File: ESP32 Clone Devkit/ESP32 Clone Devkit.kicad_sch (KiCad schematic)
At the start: 34 parts, among them J1 USB_B_Micro, J2 Conn_01x19_Pin, J3 Conn_01x19_Pin, Q1 MMSS8050-H-TP, Q2 MMSS8050-H-TP, SW1 SW_Push, SW2 SW_Push, U1 CP2102N-A02-GQFN28, U2 AMS1117-3.3

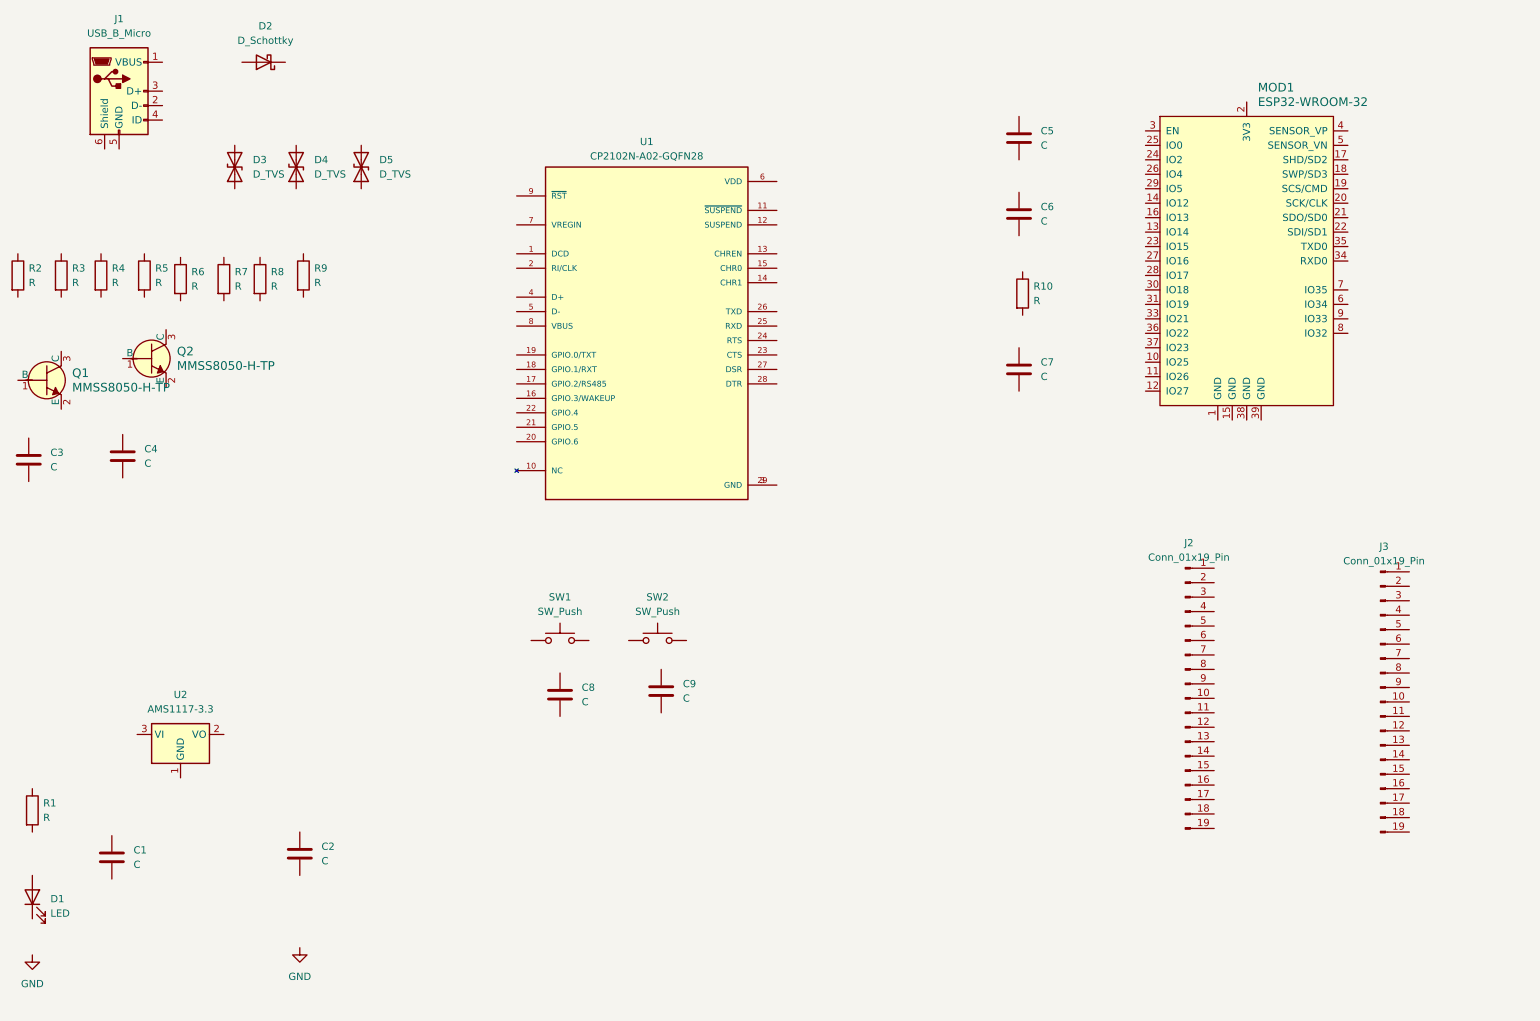
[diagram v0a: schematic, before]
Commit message: Annotate and set components values
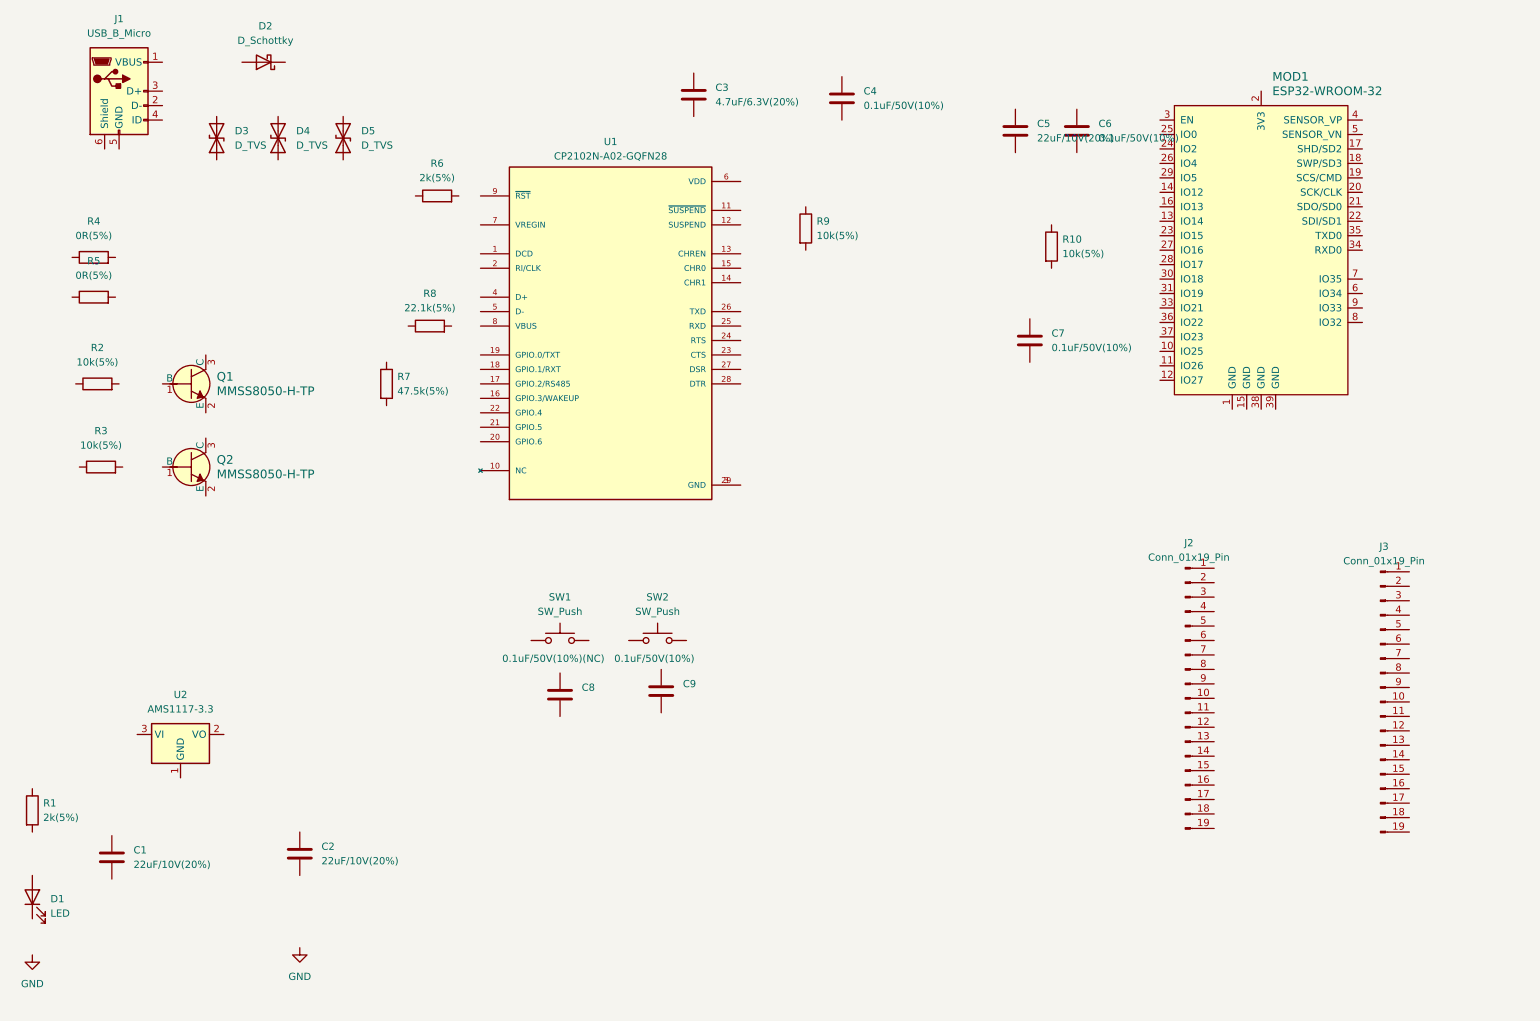
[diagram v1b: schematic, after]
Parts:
- C1, C2, C5: value C -> 22uF/10V(20%)
- C3: value C -> 4.7uF/6.3V(20%)
- C4, C6, C7, C9: value C -> 0.1uF/50V(10%)
- C8: value C -> 0.1uF/50V(10%)(NC)
- R1, R6: value R -> 2k(5%)
- R10, R2, R3, R9: value R -> 10k(5%)
- R4, R5: value R -> 0R(5%)
- R7: value R -> 47.5k(5%)
- R8: value R -> 22.1k(5%)
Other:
- moved on the sheet: C3, C4, C5, C6, C7, D3, D4, D5, MOD1, Q1, Q2, R10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

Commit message: arange components in schematic
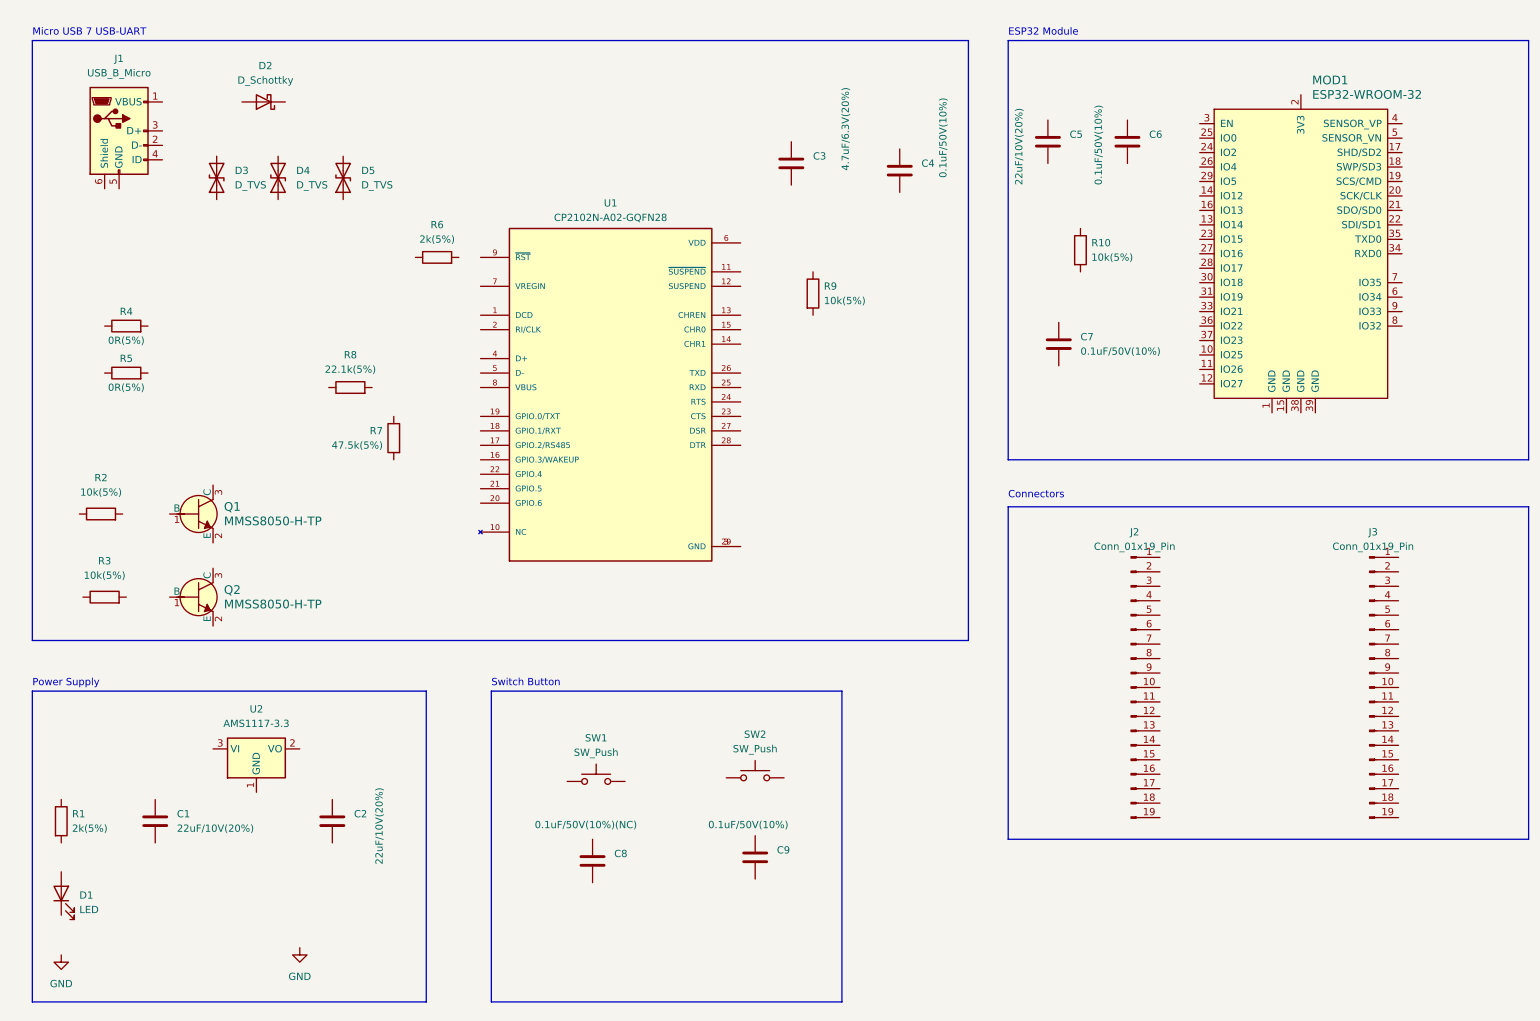
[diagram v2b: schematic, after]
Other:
- note added: "Connectors"
- note added: "ESP32 Module"
- note added: "Micro USB 7 USB-UART"
- note added: "Power Supply"
- note added: "Switch Button"
- moved on the sheet: C1, C2, C3, C4, C5, C6, C7, C8, C9, D1, D2, D3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

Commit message: associate footprints to symbols
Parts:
- C1, C2, C5: footprint (none) -> Capacitor_SMD:C_0201_0603Metric
- C3, C4, C6, C7, C8, C9: footprint (none) -> Capacitor_SMD:C_01005_0402Metric
- D1: footprint (none) -> LED_SMD:LED_0603_1608Metric
- D2: footprint (none) -> Diode_SMD:D_SOD-323
- D3, D4, D5: footprint (none) -> Diode_SMD:D_SOD-523
- J1: footprint (none) -> Connector_USB:USB_Micro-AB_Molex_47590-0001
- J2, J3: footprint (none) -> Connector_PinHeader_2.54mm:PinHeader_1x19_P2.54mm_Vertical
- R1, R10, R2, R3, R4, R5, R6, R7, R8, R9: footprint (none) -> Resistor_SMD:R_01005_0402Metric
- SW1, SW2: footprint (none) -> Button_Switch_SMD:SW_SPST_B3S-1000
- U1: footprint QFN50P500X500X80-29N -> Package_DFN_QFN:TQFN-28-1EP_5x5mm_P0.5mm_EP2.7x2.7mm
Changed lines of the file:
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@@
       (effects (font (size 1.27 1.27)) (justify left))
     )
-    (property "Footprint" "" (at 152.0952 48.895 0)
+    (property "Footprint" "Capacitor_SMD:C_01005_0402Metric" (at 152.0952 48.895 0)
       (effects (font (size 1.27 1.27)) hide)
     )
@@
       (effects (font (size 1.27 1.27)) (justify left))
     )
-    (property "Footprint" "" (at 21.082 160.655 90)
+    (property "Footprint" "Resistor_SMD:R_01005_0402Metric" (at 21.082 160.655 90)
       (effects (font (size 1.27 1.27)) hide)
     )
@@
       (effects (font (size 1.27 1.27)))
     )
-    (property "Footprint" "" (at 88.9 63.373 90)
+    (property "Footprint" "Resistor_SMD:R_01005_0402Metric" (at 88.9 63.373 90)
       (effects (font (size 1.27 1.27)) hide)
     )
@@
       (effects (font (size 1.27 1.27)) (justify left))
     )
-    (property "Footprint" "" (at 40.3352 164.465 0)
+    (property "Footprint" "Capacitor_SMD:C_0201_0603Metric" (at 40.3352 164.465 0)
       (effects (font (size 1.27 1.27)) hide)
     )
@@
       (effects (font (size 1.27 1.27)) (justify left))
     )
-    (property "Footprint" "" (at 145.7452 170.815 0)
+    (property "Footprint" "Capacitor_SMD:C_01005_0402Metric" (at 145.7452 170.815 0)
       (effects (font (size 1.27 1.27)) hide)
     )
@@
       (effects (font (size 1.27 1.27)) (justify right))
     )
-    (property "Footprint" "" (at 72.39 47.625 0)
+    (property "Footprint" "Diode_SMD:D_SOD-523" (at 72.39 47.625 0)
       (effects (font (size 1.27 1.27)) hide)
     )
@@
       (effects (font (size 1.27 1.27)))
     )
-    (property "Footprint" "" (at 116.84 148.59 0)
+    (property "Footprint" "Button_Switch_SMD:SW_SPST_B3S-1000" (at 116.84 148.59 0)
       (effects (font (size 1.27 1.27)) hide)
     )
@@
       (effects (font (size 1.27 1.27)) (justify left))
     )
-    (property "Footprint" "" (at 171.1452 50.165 0)
+    (property "Footprint" "Capacitor_SMD:C_01005_0402Metric" (at 171.1452 50.165 0)
       (effects (font (size 1.27 1.27)) hide)
     )
@@
       (effects (font (size 1.27 1.27)))
     )
-    (property "Footprint" "" (at 29.845 108.458 90)
+    (property "Footprint" "Resistor_SMD:R_01005_0402Metric" (at 29.845 108.458 90)
       (effects (font (size 1.27 1.27)) hide)
     )
@@
       (effects (font (size 1.27 1.27)) (justify left))
     )
-    (property "Footprint" "" (at 83.058 93.345 90)
+    (property "Footprint" "Resistor_SMD:R_01005_0402Metric" (at 83.058 93.345 90)
       (effects (font (size 1.27 1.27)) hide)
     )
@@
       (effects (font (size 1.27 1.27)))
     )
-    (property "Footprint" "" (at 252.73 137.16 0)
+    (property "Footprint" "Connector_PinHeader_2.54mm:PinHeader_1x19_P2.54mm_Vertical" (at 252.73 137.16 0)
       (effects (font (size 1.27 1.27)) hide)
     )
@@
       (effects (font (size 1.27 1.27)) (justify left))
     )
-    (property "Footprint" "" (at 200.152 60.325 90)
+    (property "Footprint" "Resistor_SMD:R_01005_0402Metric" (at 200.152 60.325 90)
       (effects (font (size 1.27 1.27)) hide)
     )
@@
       (effects (font (size 1.27 1.27)) (justify left))
     )
-    (property "Footprint" "" (at 199.0852 80.645 0)
+    (property "Footprint" "Capacitor_SMD:C_01005_0402Metric" (at 199.0852 80.645 0)
       (effects (font (size 1.27 1.27)) hide)
     )
@@
       (effects (font (size 1.27 1.27)))
     )
-    (property "Footprint" "QFN50P500X500X80-29N" (at 119.38 86.995 0)
+    (property "Footprint" "Package_DFN_QFN:TQFN-28-1EP_5x5mm_P0.5mm_EP2.7x2.7mm" (at 119.38 86.995 0)
       (effects (font (size 1.27 1.27)) (justify bottom) hide)
     )
@@
       (effects (font (size 1.27 1.27)))
     )
-    (property "Footprint" "" (at 144.78 147.955 0)
+    (property "Footprint" "Button_Switch_SMD:SW_SPST_B3S-1000" (at 144.78 147.955 0)
       (effects (font (size 1.27 1.27)) hide)
     )
@@
       (effects (font (size 1.27 1.27)))
     )
-    (property "Footprint" "" (at 30.48 123.063 90)
+    (property "Footprint" "Resistor_SMD:R_01005_0402Metric" (at 30.48 123.063 90)
       (effects (font (size 1.27 1.27)) hide)
     )
@@
       (effects (font (size 1.27 1.27)))
     )
-    (property "Footprint" "" (at 210.82 137.16 0)
+    (property "Footprint" "Connector_PinHeader_2.54mm:PinHeader_1x19_P2.54mm_Vertical" (at 210.82 137.16 0)
       (effects (font (size 1.27 1.27)) hide)
     )
@@
       (effects (font (size 1.27 1.27)) (justify left))
     )
-    (property "Footprint" "" (at 71.4502 164.465 0)
+    (property "Footprint" "Capacitor_SMD:C_0201_0603Metric" (at 71.4502 164.465 0)
       (effects (font (size 1.27 1.27)) hide)
     )
@@
       (effects (font (size 1.27 1.27)) (justify right))
     )
-    (property "Footprint" "" (at 50.165 47.625 0)
+    (property "Footprint" "Diode_SMD:D_SOD-523" (at 50.165 47.625 0)
       (effects (font (size 1.27 1.27)) hide)
     )
@@
       (effects (font (size 1.27 1.27)) (justify left))
     )
-    (property "Footprint" "" (at 117.1702 171.45 0)
+    (property "Footprint" "Capacitor_SMD:C_01005_0402Metric" (at 117.1702 171.45 0)
       (effects (font (size 1.27 1.27)) hide)
     )
@@
       (effects (font (size 1.27 1.27)) (justify right))
     )
-    (property "Footprint" "" (at 22.86 173.355 0)
+    (property "Footprint" "LED_SMD:LED_0603_1608Metric" (at 22.86 173.355 0)
       (effects (font (size 1.27 1.27)) hide)
     )
@@
       (effects (font (size 1.27 1.27)) (justify right))
     )
-    (property "Footprint" "" (at 60.96 47.625 0)
+    (property "Footprint" "Diode_SMD:D_SOD-523" (at 60.96 47.625 0)
       (effects (font (size 1.27 1.27)) hide)
     )
@@
       (effects (font (size 1.27 1.27)))
     )
-    (property "Footprint" "" (at 36.83 40.64 0)
+    (property "Footprint" "Connector_USB:USB_Micro-AB_Molex_47590-0001" (at 36.83 40.64 0)
       (effects (font (size 1.27 1.27)) hide)
     )
@@
       (effects (font (size 1.27 1.27)))
     )
-    (property "Footprint" "" (at 34.29 83.693 90)
+    (property "Footprint" "Resistor_SMD:R_01005_0402Metric" (at 34.29 83.693 90)
       (effects (font (size 1.27 1.27)) hide)
     )
@@
       (effects (font (size 1.27 1.27)))
     )
-    (property "Footprint" "" (at 34.29 75.438 90)
+    (property "Footprint" "Resistor_SMD:R_01005_0402Metric" (at 34.29 75.438 90)
       (effects (font (size 1.27 1.27)) hide)
     )
@@
       (effects (font (size 1.27 1.27)))
     )
-    (property "Footprint" "" (at 58.42 34.29 0)
+    (property "Footprint" "Diode_SMD:D_SOD-323" (at 58.42 34.29 0)
       (effects (font (size 1.27 1.27)) hide)
     )
@@
       (effects (font (size 1.27 1.27)) (justify left))
     )
-    (property "Footprint" "" (at 153.162 67.945 90)
+    (property "Footprint" "Resistor_SMD:R_01005_0402Metric" (at 153.162 67.945 90)
       (effects (font (size 1.27 1.27)) hide)
     )
@@
       (effects (font (size 1.27 1.27)) (justify left))
     )
-    (property "Footprint" "" (at 211.1502 45.085 0)
+    (property "Footprint" "Capacitor_SMD:C_01005_0402Metric" (at 211.1502 45.085 0)
       (effects (font (size 1.27 1.27)) hide)
     )
@@
       (effects (font (size 1.27 1.27)) (justify left))
     )
-    (property "Footprint" "" (at 197.1802 45.085 0)
+    (property "Footprint" "Capacitor_SMD:C_0201_0603Metric" (at 197.1802 45.085 0)
       (effects (font (size 1.27 1.27)) hide)
     )
@@
       (effects (font (size 1.27 1.27)))
     )
-    (property "Footprint" "" (at 73.66 86.233 90)
-      (effects (font (size 1.27 1.27)) hide)
-    )
+    (property "Footprint" "Resistor_SMD:R_01005_0402Metric" (at 73.66 86.233 90)
+      (effects (font (size 1.27 1.27)) hide)
+    )
